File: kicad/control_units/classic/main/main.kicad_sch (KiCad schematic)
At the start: 20 parts, among them J1 Conn_01x04, J2 USB_C_Receptacle_USB2.0_14P, J3 Conn_01x05, J4 Conn_01x05, J5 Conn_01x05, J6 Conn_02x05_Odd_Even, U1 STM32C552CET6, U2 AZ1117CH2-3.3, U3 TPD1E05U06DPY, U4 TPD1E05U06DPY

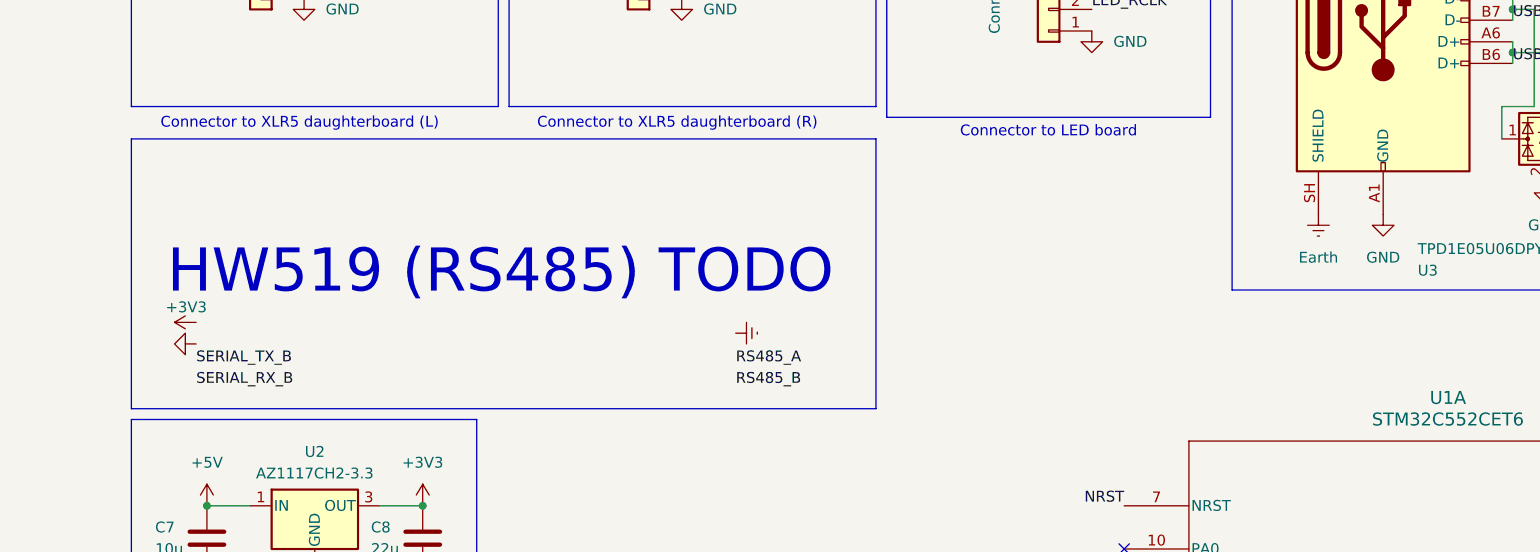
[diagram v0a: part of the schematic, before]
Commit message: feat: Should be able to footprint and route some prototype boards to see if I'm not totally off-base here
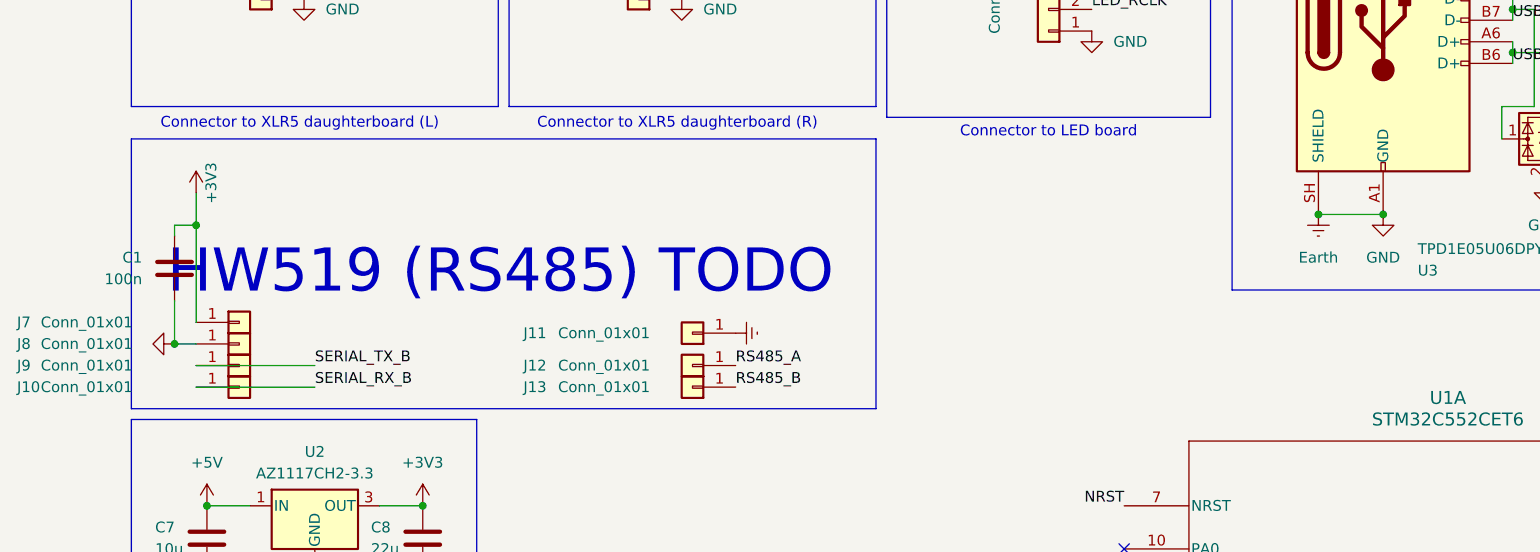
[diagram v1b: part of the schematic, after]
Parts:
- added C1: 100n, symbol Device:C
- added J10, J11, J12, J13, J7, J8, J9: Conn_01x01, symbol Connector_Generic:Conn_01x01
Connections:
- net GND is gone; now on net Earth: C11.1, C12.2, C13.1, C14.1, C15.1, C16.1, C7.1, C8.1, J1.4 (Pin_4), J2.A1 (GND), J2.A12 (GND), J2.B1 (GND), J2.B12 (GND), J3.1 (Pin_1), J4.1 (Pin_1), J5.1 (Pin_1), J6.5 (Pin_5), J6.6 (Pin_6), R1.2, R2.2, U1.23 (VSS), U1.35 (VSS), U1.47 (VSS), U1.8 (VREF-), U2.2 (GND), U3.2 (GND), U4.2 (GND)
- net +3V3: now also C1.1, J7.1 (Pin_1)
- net Earth: now also C1.2, J11.1 (Pin_1), J8.1 (Pin_1)
- net RS485_A: now also J12.1 (Pin_1)
- net RS485_B: now also J13.1 (Pin_1)
- net SERIAL_RX_B: now also J10.1 (Pin_1)
- net SERIAL_TX_B: now also J9.1 (Pin_1)

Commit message: feat: First revision of control unit main board; ignore the pad clearance violations, this shouldn't be an issue for the USB-C port specifically?
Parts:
- C1: footprint (none) -> Capacitor_THT:C_Disc_D5.0mm_W2.5mm_P2.50mm
- C11, C12, C13, C14, C15, C16: footprint Capacitor_SMD:C_0805_2012Metric -> Capacitor_THT:C_Disc_D5.0mm_W2.5mm_P2.50mm
- C7, C8: footprint Capacitor_SMD:C_0805_2012Metric -> Capacitor_THT:CP_Radial_D5.0mm_P2.50mm
- J1: footprint (none) -> Connector_PinSocket_2.54mm:PinSocket_1x04_P2.54mm_Vertical
- J10, J11, J12, J13, J7, J8, J9: footprint (none) -> Connector_PinSocket_2.54mm:PinSocket_1x01_P2.54mm_Vertical
- J3, J4, J5: footprint (none) -> Connector_PinSocket_2.54mm:PinSocket_1x05_P2.54mm_Vertical
- J6: footprint (none) -> Connector_PinSocket_2.54mm:PinSocket_2x05_P2.54mm_Vertical
- R1, R2: footprint Resistor_SMD:R_0805_2012Metric -> Resistor_THT:R_Axial_DIN0207_L6.3mm_D2.5mm_P7.62mm_Horizontal
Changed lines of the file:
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@@
 			)
 		)
-		(property "Footprint" "Capacitor_SMD:C_0805_2012Metric"
+		(property "Footprint" "Capacitor_THT:C_Disc_D5.0mm_W2.5mm_P2.50mm"
 			(at 239.7252 43.18 0)
 			(hide yes)
@@
 			)
 		)
-		(property "Footprint" ""
+		(property "Footprint" "Connector_PinSocket_2.54mm:PinSocket_1x01_P2.54mm_Vertical"
 			(at 26.67 82.55 0)
 			(hide yes)
@@
 			)
 		)
-		(property "Footprint" "Resistor_SMD:R_0805_2012Metric"
+		(property "Footprint" "Resistor_THT:R_Axial_DIN0207_L6.3mm_D2.5mm_P7.62mm_Horizontal"
 			(at 184.15 30.988 90)
 			(hide yes)
@@
 			)
 		)
-		(property "Footprint" "Capacitor_SMD:C_0805_2012Metric"
+		(property "Footprint" "Capacitor_THT:C_Disc_D5.0mm_W2.5mm_P2.50mm"
 			(at 216.2048 35.56 0)
 			(hide yes)
@@
 			)
 		)
-		(property "Footprint" ""
+		(property "Footprint" "Connector_PinSocket_2.54mm:PinSocket_1x01_P2.54mm_Vertical"
 			(at 80.01 76.2 0)
 			(hide yes)
@@
 			)
 		)
-		(property "Footprint" ""
+		(property "Footprint" "Connector_PinSocket_2.54mm:PinSocket_1x01_P2.54mm_Vertical"
 			(at 26.67 80.01 0)
 			(hide yes)
@@
 			)
 		)
-		(property "Footprint" ""
+		(property "Footprint" "Connector_PinSocket_2.54mm:PinSocket_1x05_P2.54mm_Vertical"
 			(at 73.66 31.75 0)
 			(hide yes)
@@
 			)
 		)
-		(property "Footprint" ""
+		(property "Footprint" "Connector_PinSocket_2.54mm:PinSocket_1x05_P2.54mm_Vertical"
 			(at 121.92 35.56 0)
 			(hide yes)
@@
 			)
 		)
-		(property "Footprint" ""
+		(property "Footprint" "Connector_PinSocket_2.54mm:PinSocket_1x04_P2.54mm_Vertical"
 			(at 34.29 134.62 0)
 			(hide yes)
@@
 			)
 		)
-		(property "Footprint" ""
+		(property "Footprint" "Connector_PinSocket_2.54mm:PinSocket_1x05_P2.54mm_Vertical"
 			(at 29.21 31.75 0)
 			(hide yes)
@@
 			)
 		)
-		(property "Footprint" ""
+		(property "Footprint" "Connector_PinSocket_2.54mm:PinSocket_1x01_P2.54mm_Vertical"
 			(at 26.67 77.47 0)
 			(hide yes)
@@
 			)
 		)
-		(property "Footprint" "Capacitor_SMD:C_0805_2012Metric"
+		(property "Footprint" "Capacitor_THT:C_Disc_D5.0mm_W2.5mm_P2.50mm"
 			(at 231.4448 35.56 0)
 			(hide yes)
@@
 			)
 		)
-		(property "Footprint" ""
+		(property "Footprint" "Capacitor_THT:C_Disc_D5.0mm_W2.5mm_P2.50mm"
 			(at 20.0152 72.39 0)
 			(hide yes)
@@
 			)
 		)
-		(property "Footprint" "Capacitor_SMD:C_0805_2012Metric"
+		(property "Footprint" "Capacitor_THT:CP_Radial_D5.0mm_P2.50mm"
 			(at 47.2948 96.52 0)
 			(hide yes)
@@
 			)
 		)
-		(property "Footprint" "Capacitor_SMD:C_0805_2012Metric"
+		(property "Footprint" "Capacitor_THT:CP_Radial_D5.0mm_P2.50mm"
 			(at 21.8948 96.52 0)
 			(hide yes)
@@
 			)
 		)
-		(property "Footprint" "Capacitor_SMD:C_0805_2012Metric"
+		(property "Footprint" "Capacitor_THT:C_Disc_D5.0mm_W2.5mm_P2.50mm"
 			(at 223.8248 35.56 0)
 			(hide yes)
@@
 			)
 		)
-		(property "Footprint" ""
+		(property "Footprint" "Connector_PinSocket_2.54mm:PinSocket_1x01_P2.54mm_Vertical"
 			(at 80.01 82.55 0)
 			(hide yes)
@@
 			)
 		)
-		(property "Footprint" ""
+		(property "Footprint" "Connector_PinSocket_2.54mm:PinSocket_1x01_P2.54mm_Vertical"
 			(at 26.67 74.93 0)
 			(hide yes)
@@
 			)
 		)
-		(property "Footprint" "Capacitor_SMD:C_0805_2012Metric"
+		(property "Footprint" "Capacitor_THT:C_Disc_D5.0mm_W2.5mm_P2.50mm"
 			(at 240.9952 30.48 0)
 			(hide yes)
@@
 			)
 		)
-		(property "Footprint" "Capacitor_SMD:C_0805_2012Metric"
+		(property "Footprint" "Capacitor_THT:C_Disc_D5.0mm_W2.5mm_P2.50mm"
 			(at 208.5848 35.56 0)
 			(hide yes)
@@
 			)
 		)
-		(property "Footprint" ""
+		(property "Footprint" "Connector_PinSocket_2.54mm:PinSocket_1x01_P2.54mm_Vertical"
 			(at 80.01 80.01 0)
 			(hide yes)
@@
 			)
 		)
-		(property "Footprint" "Resistor_SMD:R_0805_2012Metric"
+		(property "Footprint" "Resistor_THT:R_Axial_DIN0207_L6.3mm_D2.5mm_P7.62mm_Horizontal"
 			(at 184.15 33.528 90)
 			(hide yes)
@@
 			)
 		)
-		(property "Footprint" ""
+		(property "Footprint" "Connector_PinSocket_2.54mm:PinSocket_2x05_P2.54mm_Vertical"
 			(at 260.35 87.63 0)
 			(hide yes)
